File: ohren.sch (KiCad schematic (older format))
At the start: 30 parts, among them J1 Conn_01x19_MountingPin, U1 TLC5955RTQ

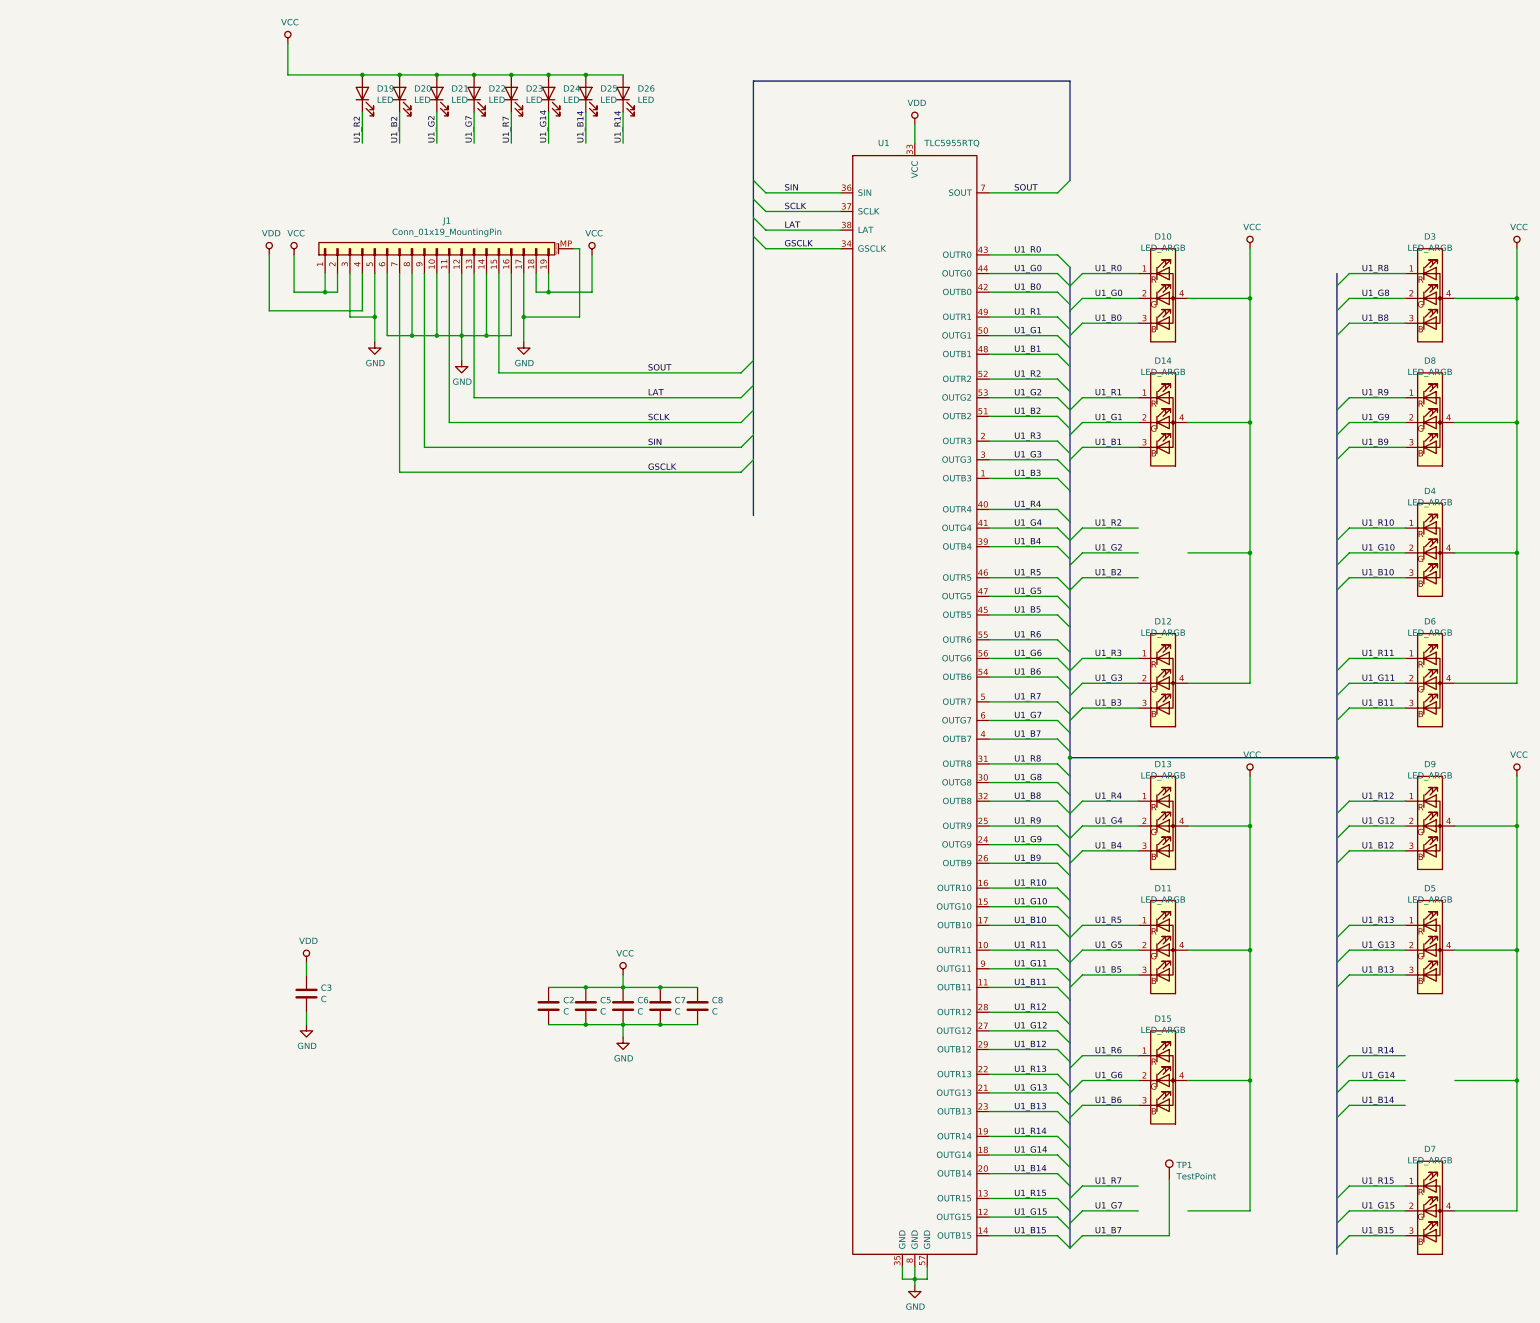
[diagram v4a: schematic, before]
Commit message: Reassign component references
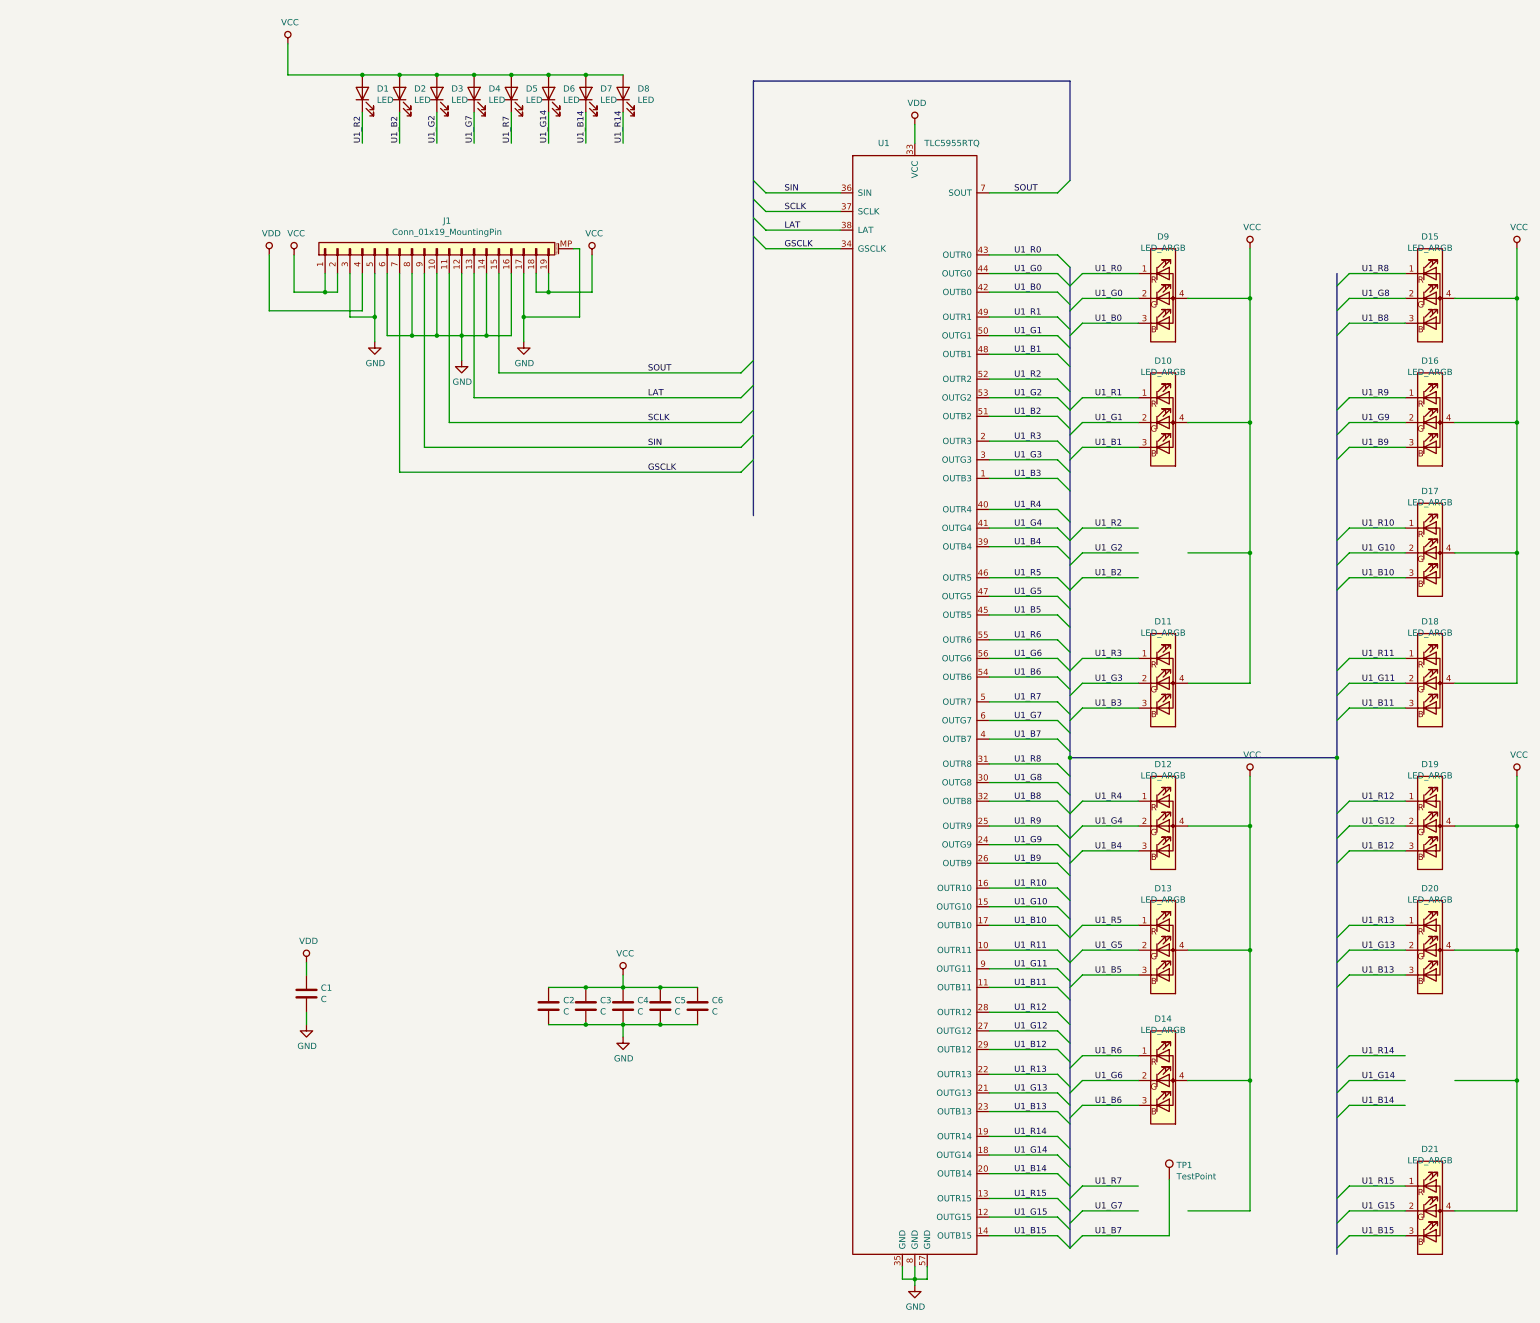
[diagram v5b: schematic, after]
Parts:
- renumbered C3 to C1, C5 to C3, C6 to C4, C7 to C5, C8 to C6, D19 to D1, D14 to D10, D12 to D11, D13 to D12, D11 to D13, D15 to D14, D3 to D15, D8 to D16, D4 to D17, D6 to D18, D9 to D19, D20 to D2, D5 to D20, D7 to D21, D21 to D3, D22 to D4, D23 to D5, D24 to D6, D25 to D7, D26 to D8, D10 to D9

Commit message: Use custom LED footprint with associated 3D model
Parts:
- D10, D11, D12, D13, D14, D15, D16, D17, D18, D19, D20, D21, D9: footprint LED_SMD:LED_Cree-PLCC4_3.2x2.8mm_CCW -> catear-pcb:ASMB-MTB1-0A3A2
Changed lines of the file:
@@
 F 0 "D18" H 10500 6597 50  0000 C CNN
 F 1 "LED_ARGB" H 10500 6506 50  0000 C CNN
-F 2 "LED_SMD:LED_Cree-PLCC4_3.2x2.8mm_CCW" H 10500 6050 50  0001 C CNN
+F 2 "catear-pcb:ASMB-MTB1-0A3A2" H 10500 6050 50  0001 C CNN
 F 3 "~" H 10500 6050 50  0001 C CNN
 	1    10500 6100
@@
 F 0 "D21" H 10500 10847 50  0000 C CNN
 F 1 "LED_ARGB" H 10500 10756 50  0000 C CNN
-F 2 "LED_SMD:LED_Cree-PLCC4_3.2x2.8mm_CCW" H 10500 10300 50  0001 C CNN
+F 2 "catear-pcb:ASMB-MTB1-0A3A2" H 10500 10300 50  0001 C CNN
 F 3 "~" H 10500 10300 50  0001 C CNN
 	1    10500 10350
@@
 F 0 "D17" H 10500 5547 50  0000 C CNN
 F 1 "LED_ARGB" H 10500 5456 50  0000 C CNN
-F 2 "LED_SMD:LED_Cree-PLCC4_3.2x2.8mm_CCW" H 10500 5000 50  0001 C CNN
+F 2 "catear-pcb:ASMB-MTB1-0A3A2" H 10500 5000 50  0001 C CNN
 F 3 "~" H 10500 5000 50  0001 C CNN
 	1    10500 5050
@@
 F 0 "D20" H 10500 8747 50  0000 C CNN
 F 1 "LED_ARGB" H 10500 8656 50  0000 C CNN
-F 2 "LED_SMD:LED_Cree-PLCC4_3.2x2.8mm_CCW" H 10500 8200 50  0001 C CNN
+F 2 "catear-pcb:ASMB-MTB1-0A3A2" H 10500 8200 50  0001 C CNN
 F 3 "~" H 10500 8200 50  0001 C CNN
 	1    10500 8250
@@
 F 0 "D16" H 10500 4497 50  0000 C CNN
 F 1 "LED_ARGB" H 10500 4406 50  0000 C CNN
-F 2 "LED_SMD:LED_Cree-PLCC4_3.2x2.8mm_CCW" H 10500 3950 50  0001 C CNN
+F 2 "catear-pcb:ASMB-MTB1-0A3A2" H 10500 3950 50  0001 C CNN
 F 3 "~" H 10500 3950 50  0001 C CNN
 	1    10500 4000
@@
 F 0 "D19" H 10500 7747 50  0000 C CNN
 F 1 "LED_ARGB" H 10500 7656 50  0000 C CNN
-F 2 "LED_SMD:LED_Cree-PLCC4_3.2x2.8mm_CCW" H 10500 7200 50  0001 C CNN
+F 2 "catear-pcb:ASMB-MTB1-0A3A2" H 10500 7200 50  0001 C CNN
 F 3 "~" H 10500 7200 50  0001 C CNN
 	1    10500 7250
@@
 F 0 "D9" H 8350 3497 50  0000 C CNN
 F 1 "LED_ARGB" H 8350 3406 50  0000 C CNN
-F 2 "LED_SMD:LED_Cree-PLCC4_3.2x2.8mm_CCW" H 8350 2950 50  0001 C CNN
+F 2 "catear-pcb:ASMB-MTB1-0A3A2" H 8350 2950 50  0001 C CNN
 F 3 "~" H 8350 2950 50  0001 C CNN
 	1    8350 3000
@@
 F 0 "D13" H 8350 8747 50  0000 C CNN
 F 1 "LED_ARGB" H 8350 8656 50  0000 C CNN
-F 2 "LED_SMD:LED_Cree-PLCC4_3.2x2.8mm_CCW" H 8350 8200 50  0001 C CNN
+F 2 "catear-pcb:ASMB-MTB1-0A3A2" H 8350 8200 50  0001 C CNN
 F 3 "~" H 8350 8200 50  0001 C CNN
 	1    8350 8250
@@
 F 0 "D10" H 8350 4497 50  0000 C CNN
 F 1 "LED_ARGB" H 8350 4406 50  0000 C CNN
-F 2 "LED_SMD:LED_Cree-PLCC4_3.2x2.8mm_CCW" H 8350 3950 50  0001 C CNN
+F 2 "catear-pcb:ASMB-MTB1-0A3A2" H 8350 3950 50  0001 C CNN
 F 3 "~" H 8350 3950 50  0001 C CNN
 	1    8350 4000
@@
 F 0 "D14" H 8350 9797 50  0000 C CNN
 F 1 "LED_ARGB" H 8350 9706 50  0000 C CNN
-F 2 "LED_SMD:LED_Cree-PLCC4_3.2x2.8mm_CCW" H 8350 9250 50  0001 C CNN
+F 2 "catear-pcb:ASMB-MTB1-0A3A2" H 8350 9250 50  0001 C CNN
 F 3 "~" H 8350 9250 50  0001 C CNN
 	1    8350 9300
@@
 F 0 "D11" H 8350 6597 50  0000 C CNN
 F 1 "LED_ARGB" H 8350 6506 50  0000 C CNN
-F 2 "LED_SMD:LED_Cree-PLCC4_3.2x2.8mm_CCW" H 8350 6050 50  0001 C CNN
+F 2 "catear-pcb:ASMB-MTB1-0A3A2" H 8350 6050 50  0001 C CNN
 F 3 "~" H 8350 6050 50  0001 C CNN
 	1    8350 6100
@@
 F 0 "D12" H 8350 7747 50  0000 C CNN
 F 1 "LED_ARGB" H 8350 7656 50  0000 C CNN
-F 2 "LED_SMD:LED_Cree-PLCC4_3.2x2.8mm_CCW" H 8350 7200 50  0001 C CNN
+F 2 "catear-pcb:ASMB-MTB1-0A3A2" H 8350 7200 50  0001 C CNN
 F 3 "~" H 8350 7200 50  0001 C CNN
 	1    8350 7250
@@
 F 0 "D15" H 10500 3497 50  0000 C CNN
 F 1 "LED_ARGB" H 10500 3406 50  0000 C CNN
-F 2 "LED_SMD:LED_Cree-PLCC4_3.2x2.8mm_CCW" H 10500 2950 50  0001 C CNN
+F 2 "catear-pcb:ASMB-MTB1-0A3A2" H 10500 2950 50  0001 C CNN
 F 3 "~" H 10500 2950 50  0001 C CNN
 	1    10500 3000
